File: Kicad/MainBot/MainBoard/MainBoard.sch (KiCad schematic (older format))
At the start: 89 parts, among them J1 Conn_01x02, J10 Conn_01x24, J11 01x24, J12 Conn_01x05, J13 Conn_01x03, J14 Conn_01x03, J15 Conn_01x03, J16 01x04, J17 01x04, J18 01x04, J19 01x04, J20 Conn_01x03, U1 AZ1117-3.3, U2 TCA9548A, U3 Teensy3.6, U4 DRV8825, U5 DRV8825, U6 DRV8825, U7 DRV8825

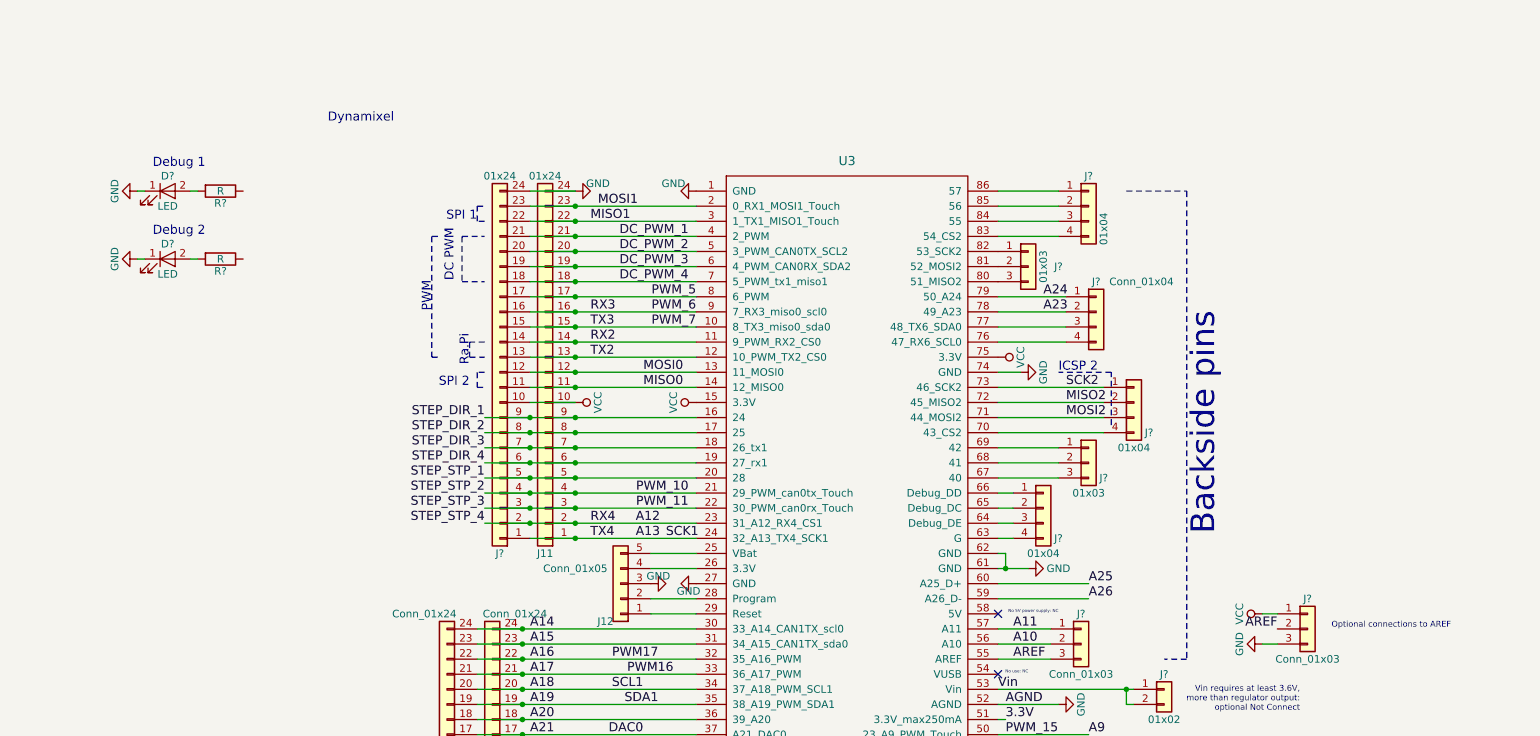
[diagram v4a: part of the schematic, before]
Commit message: Added Serial channel to Dynamixel actuators, connected debug LEDs to Teensy
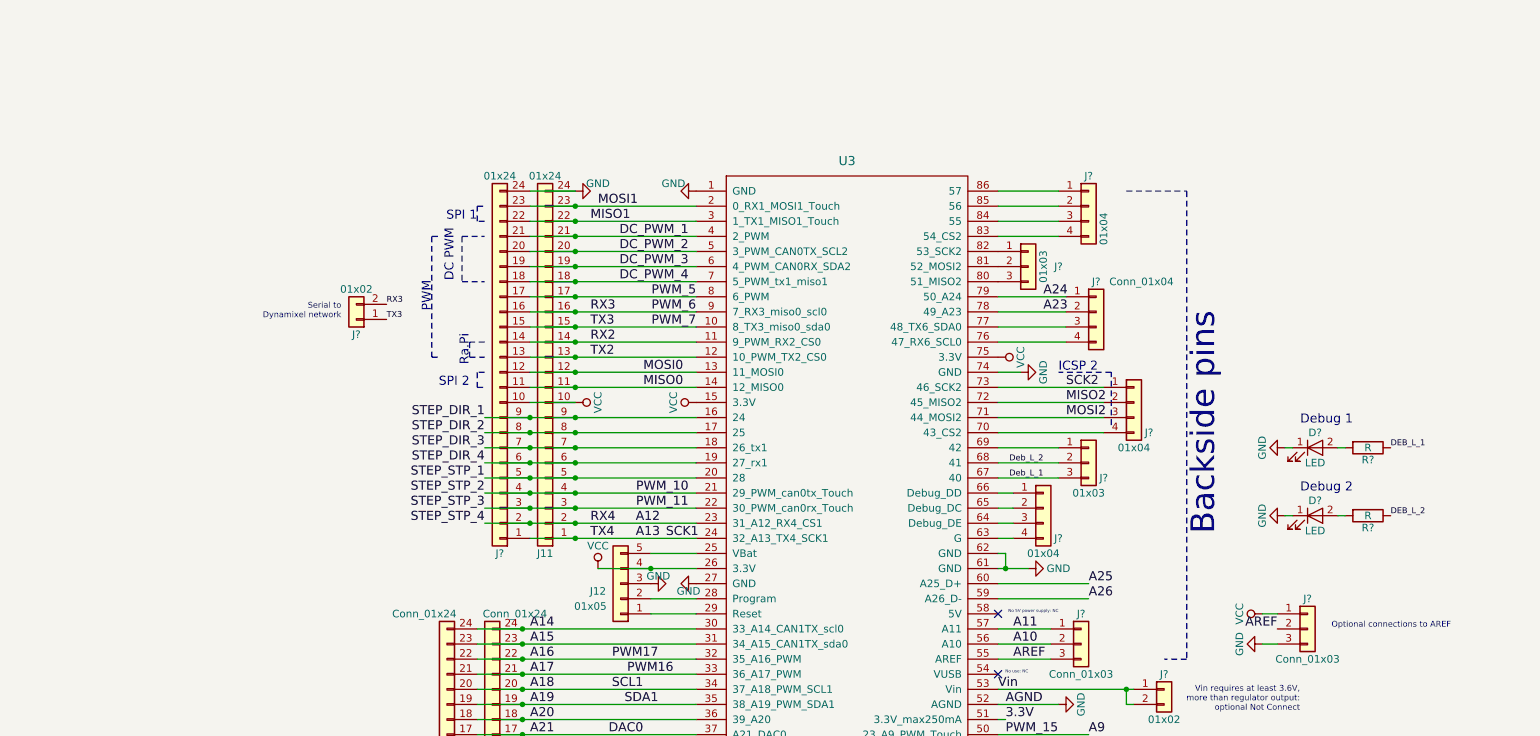
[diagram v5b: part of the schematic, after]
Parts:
- added J?: 01x02, symbol Conn_01x02
- J12: value Conn_01x05 -> 01x05
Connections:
- net PWM_6: now also J?.2 (Pin_2)
- net PWM_7: now also J?.1 (Pin_1)
- net VCC: now also J12.4 (Pin_4), U3.26 (3.3V)
- net Deb_L_1: now reaches J?.3 (Pin_3), U3.67 (40)
- net Deb_L_2: now reaches J?.2 (Pin_2), U3.68 (41)
- net DEB_L_1: now reaches R?.1
- net DEB_L_2: now reaches R?.1
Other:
- note added: "Serial to \nDynamixel network"
- note removed: "Dynamixel\n"
- moved on the sheet: D?, R?
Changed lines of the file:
@@
 U 1 1 5C620E53
 P 6800 5700
-F 0 "J12" H 6900 5950 50  0000 C CNN
-F 1 "Conn_01x05" H 7100 5600 50  0000 C CNN
+F 0 "J12" H 6950 5750 50  0000 C CNN
+F 1 "01x05" H 7000 5850 50  0000 C CNN
 F 2 "Pin_Headers:Pin_Header_Straight_1x05_Pitch2.54mm" H 6800 5700 50  0001 C CNN
 F 3 "" H 6800 5700 50  0001 C CNN
@@
 	7000 5500 7300 5500
 Wire Wire Line
-	7000 5600 7300 5600
-Wire Wire Line
 	7000 5800 7300 5800
 Wire Wire Line
@@
 L LED D?
 U 1 1 5C78FE4B
-P 3800 3100
-F 0 "D?" H 3800 3200 50  0000 C CNN
-F 1 "LED" H 3800 3000 50  0000 C CNN
-F 2 "" H 3800 3100 50  0001 C CNN
-F 3 "" H 3800 3100 50  0001 C CNN
-	1    3800 3100
+P 11400 4800
+F 0 "D?" H 11400 4900 50  0000 C CNN
+F 1 "LED" H 11400 4700 50  0000 C CNN
+F 2 "" H 11400 4800 50  0001 C CNN
+F 3 "" H 11400 4800 50  0001 C CNN
+	1    11400 4800
 	1    0    0    -1
 $EndComp
@@
 L R R?
 U 1 1 5C790048
-P 4150 3100
-F 0 "R?" V 4230 3100 50  0000 C CNN
-F 1 "R" V 4150 3100 50  0000 C CNN
-F 2 "" V 4080 3100 50  0001 C CNN
-F 3 "" H 4150 3100 50  0001 C CNN
-	1    4150 3100
+P 11750 4800
+F 0 "R?" V 11830 4800 50  0000 C CNN
+F 1 "R" V 11750 4800 50  0000 C CNN
+F 2 "" V 11680 4800 50  0001 C CNN
+F 3 "" H 11750 4800 50  0001 C CNN
+	1    11750 4800
 	0    1    1    0
 $EndComp
@@
 L GND #PWR?
 U 1 1 5C7907E8
-P 3600 3100
-F 0 "#PWR?" H 3600 2850 50  0001 C CNN
-F 1 "GND" H 3600 2950 50  0000 C CNN
-F 2 "" H 3600 3100 50  0001 C CNN
-F 3 "" H 3600 3100 50  0001 C CNN
-	1    3600 3100
+P 11200 4800
+F 0 "#PWR?" H 11200 4550 50  0001 C CNN
+F 1 "GND" H 11200 4650 50  0000 C CNN
+F 2 "" H 11200 4800 50  0001 C CNN
+F 3 "" H 11200 4800 50  0001 C CNN
+	1    11200 4800
 	0    1    1    0
 $EndComp
@@
 	3100 1500 3050 1500
 Wire Wire Line
-	3600 3100 3650 3100
+	11200 4800 11250 4800
 Wire Wire Line
 	2750 1500 2700 1500
 Wire Wire Line
-	3950 3100 4000 3100
+	11550 4800 11600 4800
 $Comp
 L VCC #PWR?
@@
 Text Notes 15500 6500 2    60   ~ 0
 Steppers Fault Pins\n
-Text Notes 4050 2950 2    60   ~ 0
+Text Notes 11650 4650 2    60   ~ 0
 Debug 1\n
-Text Notes 4050 3400 2    60   ~ 0
+Text Notes 11650 5100 2    60   ~ 0
 Debug 2\n
 $Comp
 L LED D?
 U 1 1 5C7A0281
-P 3800 3550
-F 0 "D?" H 3800 3650 50  0000 C CNN
-F 1 "LED" H 3800 3450 50  0000 C CNN
-F 2 "" H 3800 3550 50  0001 C CNN
-F 3 "" H 3800 3550 50  0001 C CNN
-	1    3800 3550
+P 11400 5250
+F 0 "D?" H 11400 5350 50  0000 C CNN
+F 1 "LED" H 11400 5150 50  0000 C CNN
+F 2 "" H 11400 5250 50  0001 C CNN
+F 3 "" H 11400 5250 50  0001 C CNN
+	1    11400 5250
 	1    0    0    -1
 $EndComp
@@
 L R R?
 U 1 1 5C7A0287
-P 4150 3550
-F 0 "R?" V 4230 3550 50  0000 C CNN
-F 1 "R" V 4150 3550 50  0000 C CNN
-F 2 "" V 4080 3550 50  0001 C CNN
-F 3 "" H 4150 3550 50  0001 C CNN
-	1    4150 3550
+P 11750 5250
+F 0 "R?" V 11830 5250 50  0000 C CNN
+F 1 "R" V 11750 5250 50  0000 C CNN
+F 2 "" V 11680 5250 50  0001 C CNN
+F 3 "" H 11750 5250 50  0001 C CNN
+	1    11750 5250
 	0    1    1    0
 $EndComp
@@
 L GND #PWR?
 U 1 1 5C7A028D
-P 3600 3550
-F 0 "#PWR?" H 3600 3300 50  0001 C CNN
-F 1 "GND" H 3600 3400 50  0000 C CNN
-F 2 "" H 3600 3550 50  0001 C CNN
-F 3 "" H 3600 3550 50  0001 C CNN
-	1    3600 3550
-	0    1    1    0
-$EndComp
-Wire Wire Line
-	3600 3550 3650 3550
-Wire Wire Line
-	3950 3550 4000 3550
-Text Notes 5300 2650 2    60   ~ 0
-Dynamixel\n
+P 11200 5250
+F 0 "#PWR?" H 11200 5000 50  0001 C CNN
+F 1 "GND" H 11200 5100 50  0000 C CNN
+F 2 "" H 11200 5250 50  0001 C CNN
+F 3 "" H 11200 5250 50  0001 C CNN
+	1    11200 5250
+	0    1    1    0
+$EndComp
+Wire Wire Line
+	11200 5250 11250 5250
+Wire Wire Line
+	11550 5250 11600 5250
 Text Label 6950 6700 2    60   ~ 0
 DAC0
@@
 Text Notes 9500 6300 2    20   ~ 0
 No use: NC
+$Comp
+L VCC #PWR?
+U 1 1 5C7C65B9
+P 6650 5600
+F 0 "#PWR?" H 6650 5450 50  0001 C CNN
+F 1 "VCC" H 6650 5750 50  0000 C CNN
+F 2 "" H 6650 5600 50  0001 C CNN
+F 3 "" H 6650 5600 50  0001 C CNN
+	1    6650 5600
+	1    0    0    -1
+$EndComp
+Wire Wire Line
+	6650 5600 7300 5600
+Connection ~ 7000 5600
+Text Label 9600 5000 2    39   ~ 0
+Deb_L_1
+Text Label 9600 4900 2    39   ~ 0
+Deb_L_2
+Text Label 11900 4800 0    39   ~ 0
+DEB_L_1
+Text Label 11900 5250 0    39   ~ 0
+DEB_L_2
+$Comp
+L Conn_01x02 J?
+U 1 1 5C7CA251
+P 5050 3950
+F 0 "J?" H 5050 4050 50  0000 C CNN
+F 1 "01x02" H 5050 3750 50  0000 C CNN
+F 2 "" H 5050 3950 50  0001 C CNN
+F 3 "" H 5050 3950 50  0001 C CNN
+	1    5050 3950
+	-1   0    0    1
+$EndComp
+Text Label 5250 3850 0    39   ~ 0
+RX3
+Text Label 5250 3950 0    39   ~ 0
+TX3
+Text Notes 4950 3950 2    39   ~ 0
+Serial to \nDynamixel network
 $EndSCHEMATC

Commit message: Removed Dynamixel connectors
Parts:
- removed J?: Conn_01x03, symbol Conn_01x03
- removed J?: 01x04, symbol Conn_01x04
- removed J?: 01x02, symbol Conn_01x02
- added J13: 01x02, symbol Conn_01x02
- added J22: Conn_01x03, symbol Conn_01x03
- added J28: Conn_01x02, symbol Conn_01x02
- gave numbers to parts that had none: 60
- renumbered J1 to J12, J10 to J17, J11 to J19, J12 to J20, J13 to J30, J14 to J43, J15 to J48, J20 to J50, J16 to J51, J17 to J52, J18 to J53, J19 to J54, R1 to R18, R2 to R19, Tantalum to Tantalum1, Tantalum to Tantalum2
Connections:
- net RX_2 is gone; now on net RX2: J12.2 (Pin_2)
- net TX_2 is gone; now on net TX2: J12.1 (Pin_1)
- net GND: now also J13.2 (Pin_2)
- net Vin: no longer U3.53 (Vin)
- net at U3.64 (Debug_DE): now also J22.3 (Pin_3)
- net at U3.65 (Debug_DC): now also J22.2 (Pin_2)
- net at U3.66 (Debug_DD): now also J22.1 (Pin_1)
- removed net +12V: C4.2, Tantalum1.2, U1.3 (VI), U4.~ (VMOT), U5.~ (VMOT), U6.~ (VMOT), U7.~ (VMOT)
- net A25: no longer names the net of U3.60 (A25_D+)
- net A26: no longer names the net of U3.59 (A26_D-)
- new net: J28.1 (Pin_1), J28.2 (Pin_2), U3.53 (Vin)
- new net +12C: C4.2, J13.1 (Pin_1), Tantalum1.2, U1.3 (VI), U4.~ (VMOT), U5.~ (VMOT), U6.~ (VMOT), U7.~ (VMOT)
- no-connect marks 5 -> 8
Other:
- note added: "+vcc gnd\n"
- note added: "anti pola inverse\n"
- note added: "check\n"
- note added: "mosfet ou diode\n"
- note added: "pull-up\n"
- note added: "rpi\n"
- note removed: "Optional connections to AREF\n"
- note removed: "Vin requires at least 3.6V, \nmore than regulator output:\n optional Not Connect"
- moved on the sheet: J15

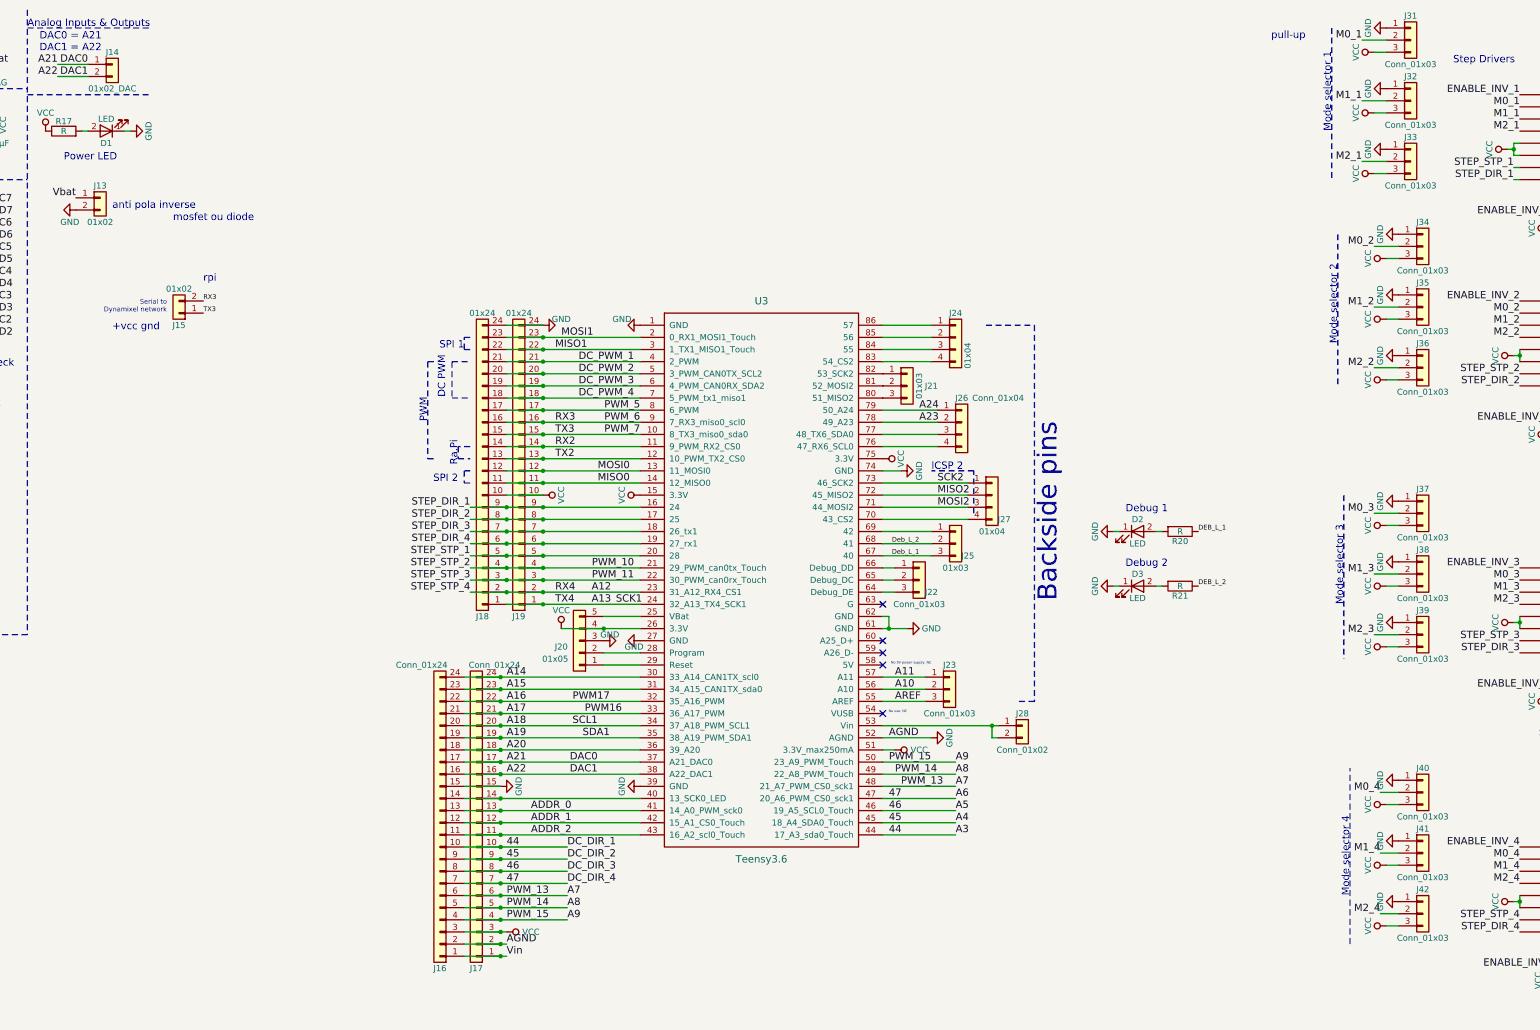
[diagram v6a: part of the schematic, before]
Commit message: Redesigned Steppers' mode selectors
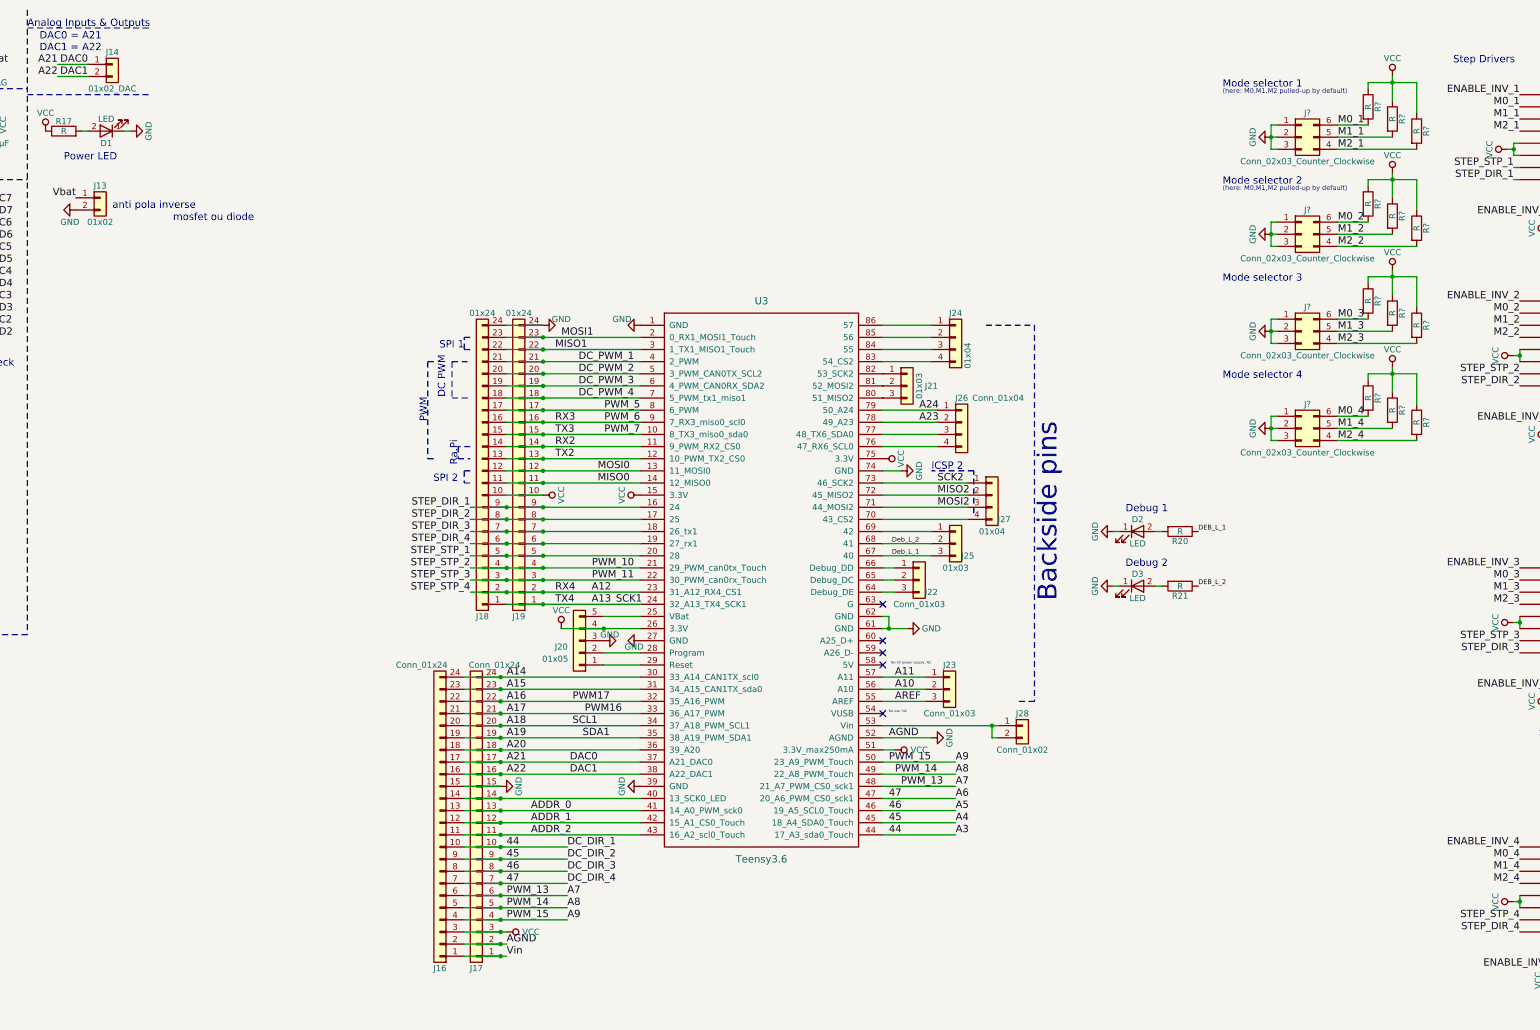
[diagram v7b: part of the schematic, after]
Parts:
- removed J15: 01x02, symbol Conn_01x02
- removed J31, J32, J33, J34, J35, J36, J37, J38, J39, J40, J41, J42: Conn_01x03, symbol Conn_01x03
- added J? (x4): Conn_02x03_Counter_Clockwise, symbol Conn_02x03_Counter_Clockwise
- added R? (x12): R, symbol R
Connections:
- net GND: now also J?.1 (Pin_1), J?.1 (Pin_1), J?.1 (Pin_1), J?.1 (Pin_1), J?.2 (Pin_2), J?.2 (Pin_2), J?.2 (Pin_2), J?.2 (Pin_2), J?.3 (Pin_3), J?.3 (Pin_3), J?.3 (Pin_3), J?.3 (Pin_3)
- net M0_1: now also J?.6 (Pin_6), R?.2
- net M0_2: now also J?.6 (Pin_6), R?.2
- net M0_3: now also J?.6 (Pin_6), R?.2
- net M0_4: now also J?.6 (Pin_6), R?.2
- net M1_1: now also J?.5 (Pin_5), R?.2
- net M1_2: now also J?.5 (Pin_5), R?.2
- net M1_3: now also J?.5 (Pin_5), R?.2
- net M1_4: now also J?.5 (Pin_5), R?.2
- net M2_1: now also J?.4 (Pin_4), R?.2
- net M2_2: now also J?.4 (Pin_4), R?.2
- net M2_3: now also J?.4 (Pin_4), R?.2
- net M2_4: now also J?.4 (Pin_4), R?.2
- net VCC: now also R?.1, R?.1, R?.1, R?.1, R?.1, R?.1, R?.1, R?.1, R?.1, R?.1, R?.1, R?.1
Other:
- note added: "(here: M0,M1,M2 pulled-up by default)"
- note added: "Mode selector 1"
- note added: "Mode selector 4"
- note removed: "Mode selector 1\n"
- note removed: "Mode selector 4\n"
- note removed: "Serial to \nDynamixel network"
- note removed: "pull-up\n"
- note removed: "rpi\n"

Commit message: Corrected multiplexer connectors to slaves
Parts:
- removed J10, J11, J4, J5, J6, J7, J8, J9: 01x04, symbol Conn_01x04
- added J? (x8): Conn_01x04, symbol Conn_01x04
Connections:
- net GND: now also J?.4 (Pin_4), J?.4 (Pin_4), J?.4 (Pin_4), J?.4 (Pin_4), J?.4 (Pin_4), J?.4 (Pin_4), J?.4 (Pin_4), J?.4 (Pin_4)
- net M_SC0: now also J?.2 (Pin_2)
- net M_SC1: now also J?.2 (Pin_2)
- net M_SC2: now also J?.2 (Pin_2)
- net M_SC3: now also J?.2 (Pin_2)
- net M_SC4: now also J?.2 (Pin_2)
- net M_SC5: now also J?.2 (Pin_2)
- net M_SC6: now also J?.2 (Pin_2)
- net M_SC7: now also J?.2 (Pin_2)
- net M_SD0: now also J?.3 (Pin_3)
- net M_SD1: now also J?.3 (Pin_3)
- net M_SD2: now also J?.3 (Pin_3)
- net M_SD3: now also J?.3 (Pin_3)
- net M_SD4: now also J?.3 (Pin_3)
- net M_SD5: now also J?.3 (Pin_3)
- net M_SD6: now also J?.3 (Pin_3)
- net M_SD7: now also J?.3 (Pin_3)
- net VCC: now also J?.1 (Pin_1), J?.1 (Pin_1), J?.1 (Pin_1), J?.1 (Pin_1), J?.1 (Pin_1), J?.1 (Pin_1), J?.1 (Pin_1), J?.1 (Pin_1)
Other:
- note removed: "check\n"
- moved on the sheet: J1, J2, J3
